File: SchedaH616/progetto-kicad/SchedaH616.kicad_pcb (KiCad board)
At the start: 6 copper layers, 50 x 70 mm, 364 parts, among them J1 BUS_POWER_MIKILAB, J103 DC-005-5A-2.0, J104 TYPE-C-31-M-12, J2 BUS_MIKILAB_MAIN, J301 UART0 debug, J401 DM3AT-SF-PEJM5, J501 HR911130C, J601 U.FL, J701 SMA antenna, J702 SMA PPS OUT, J703 SMA STROBE IN, J704 PPS/STROBE, J801 TYPE-C-31-M-12, SW301 RESET, SW302 FEL, U101 TPS56637RPAR, U103 TPS2121RUXR, U104 FUSB302BMPX, U105 SY6280AAC, U106 TPS259470ARPWR, U107 TPD2EUSB30ADRTR, U108 TPS2121RUXR, U201 AXP313A, U202 TPS563201DDCR, U203 AP2112K-1.8TRG1, U301 H616, U302 TPD4E05U06DQA, U303 TPD4E05U06DQA, U304 TPD4E05U06DQA, U305 TPD4E05U06DQA, U306 TPD4E05U06DQA, U307 TPD4E05U06DQA, U308 TCA6416APWR, U401 MT53E512M32D1ZW-046 IT:B, U402 FEMDNN064G-C9A61, U403 TPD4E05U06DQA, U404 TPD4E05U06DQA, U501 RTL8211F-CG, U502 25AA02E48T-I/OT, U601 AP6256, U701 NEO-M9N-00B, U702 74LVC1G17, U703 74LVC1G17, U801 TPS2553DBVR, U802 USBLC6-2SC6, Y301 24MHz, Y501 25MHz

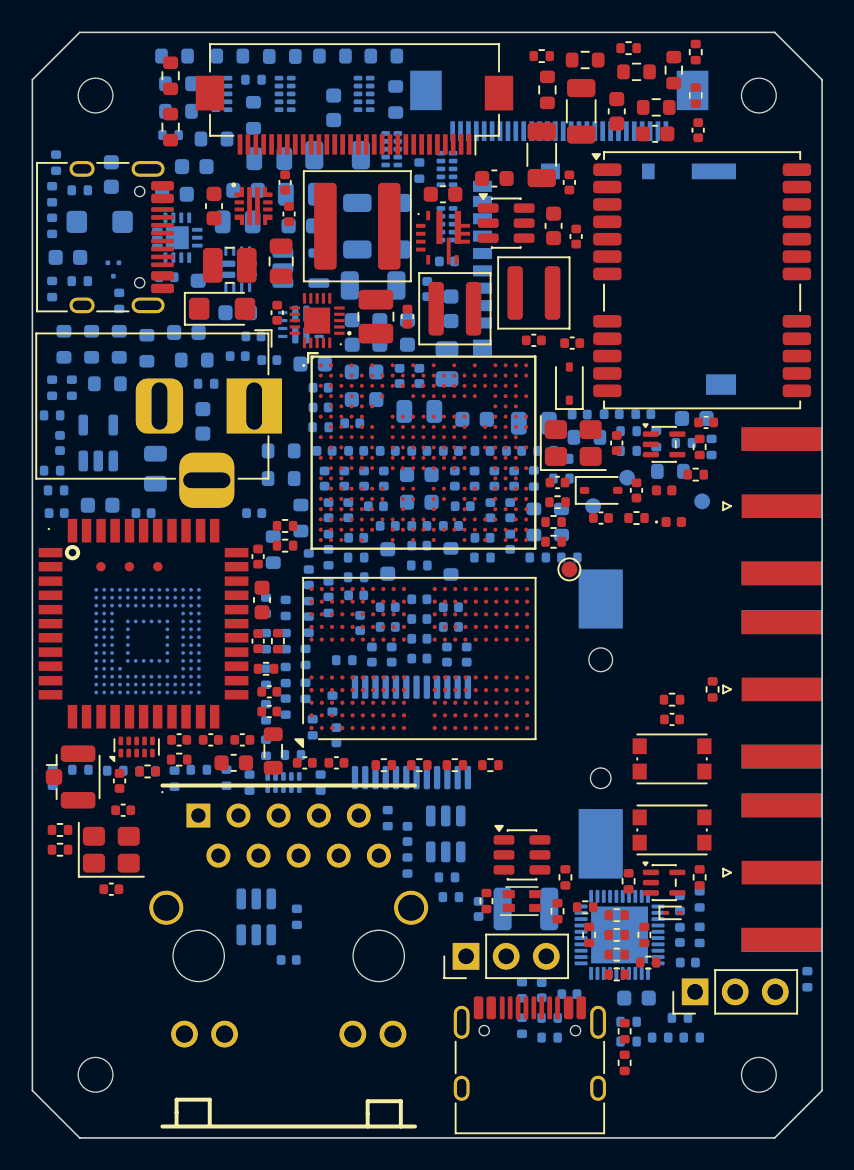
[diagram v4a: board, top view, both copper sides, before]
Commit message: SchedaH616: eFuse TPS259470 eliminato
- tolti U106 TPS259470 e i suoi componenti (partitore UVLO/OVLO, RILM, dVdT, 1 uF d'ingresso) e il footprint RPW dalla libreria
- VIN_SYS dal BUS_POWER direttamente all'ingresso del TPS56637 (restano C101/C102 10 uF e C125 100 nF)
- ingresso 12 V senza limite di corrente, OVP ne' blocco inverso; nessuna TVS sui 12 V
- P17 del TCA6416A ora libera; documenti aggiornati
- ERC 0, parita' 0, DRC 0 (solo collegamenti da fare)

Co-Authored-By: Claude Opus 5.5 (1M context) <noreply@anthropic.com>
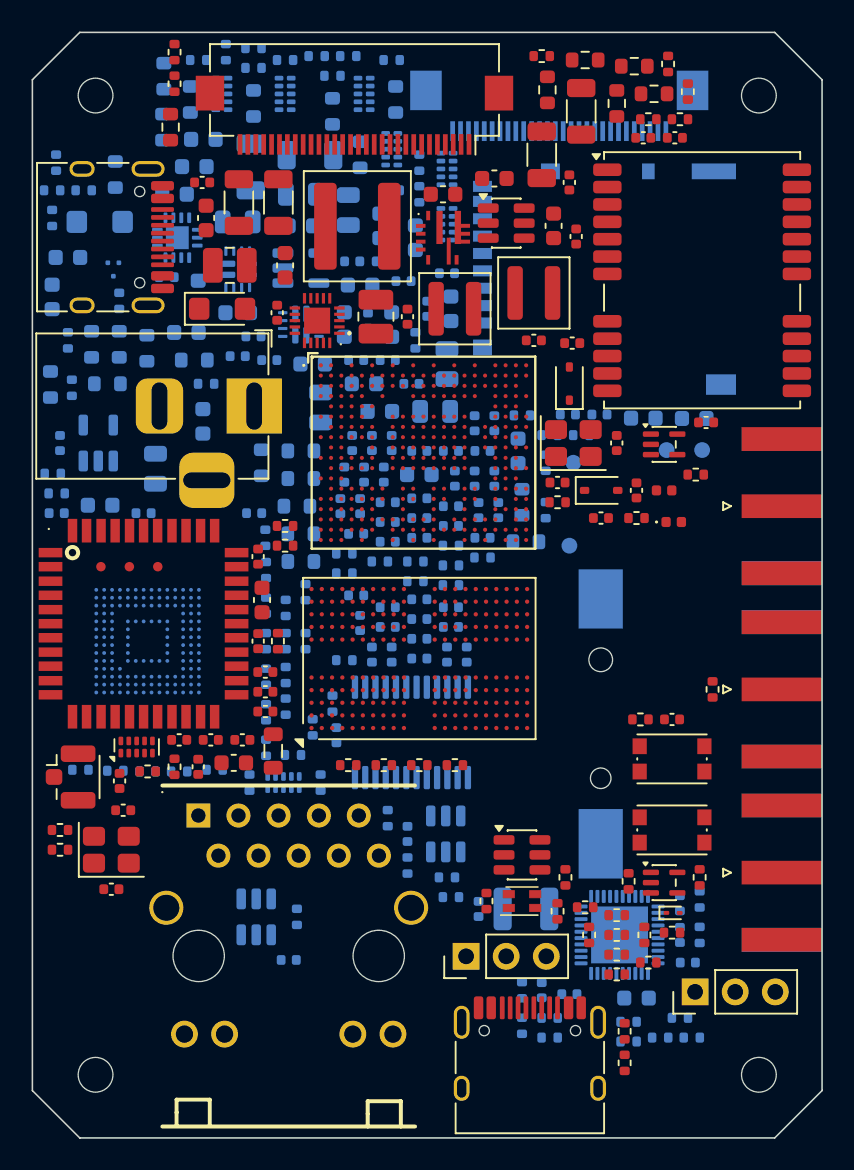
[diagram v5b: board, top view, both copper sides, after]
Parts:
- removed C130: 22nF, Capacitor_SMD:C_0603_1608Metric
- removed C131: 1uF/25V, Capacitor_SMD:C_0805_2012Metric
- removed R117: 430k 1%, Resistor_SMD:R_0603_1608Metric
- removed R118: 22k 1%, Resistor_SMD:R_0603_1608Metric
- removed R119: 39k 1%, Resistor_SMD:R_0603_1608Metric
- removed R120: 1.11k 1%, Resistor_SMD:R_0603_1608Metric
- removed R335: 10k, Resistor_SMD:R_0402_1005Metric
- removed U106: TPS259470ARPWR, H616:Texas_RPW0010A_VQFN-HR-10_2x2mm_P0.5mm
- C104, C105, C201, C208, C418, C423, R114, R3, R312, R314, R317, R318, R327, R414, R419, R705: moved to F.Cu
- C126, C205, C422, C705, R103, R104, R203, R204, R205, R334, R336, R408, R409, R416, TP101: moved to B.Cu
- moved R4 39.6 mm to (101.1, 122.3), turned to 90 degrees
- moved R324 38.0 mm to (101.5, 108.2), turned to 90 degrees
- moved R336 37.1 mm to (101.3, 111.8), turned to 90 degrees
- moved R127 30.7 mm to (131.0, 129.8)
- moved R312 24.4 mm to (132.2, 101.5)
- moved R104 24.3 mm to (114.0, 104.5), turned to 90 degrees
- moved R311 23.6 mm to (122.8, 101.8)
- moved R205 23.0 mm to (119.0, 102.8), turned to 0 degrees
- moved R327 22.5 mm to (141.5, 103.8)
- moved R318 22.2 mm to (109.0, 101.2)
- moved R3 22.2 mm to (139.4, 103.9)
- moved R314 22.0 mm to (139.0, 105.5)
- moved R310 21.6 mm to (120.0, 101.5), turned to 0 degrees
- moved R326 20.8 mm to (141.0, 105.5), turned to 0 degrees
- moved R607 19.2 mm to (101.3, 127.9), turned to 0 degrees
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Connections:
- C101 pad 1: /Alimentazione/VIN_12V -> /VIN_SYS
- C102 pad 1: /Alimentazione/VIN_12V -> /VIN_SYS
- C125 pad 1: /Alimentazione/VIN_12V -> /VIN_SYS
- R101 pad 1: /Alimentazione/VIN_12V -> /VIN_SYS
- U101 pad 8: /Alimentazione/VIN_12V -> /VIN_SYS
- U308 pad 20: /EFUSE_FLT_N -> unconnected-(U308-P17-Pad20)
